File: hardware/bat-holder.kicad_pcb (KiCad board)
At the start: 2 copper layers, 85 x 56 mm, 30 parts, among them J101 BAT_1049P, K101 BAT, K102 NTC, P101 C, Q101 NPN, Q102 NPN, Q103 DMP2035UVTQ, Q104 DMP2035UVTQ, U101 AP9211

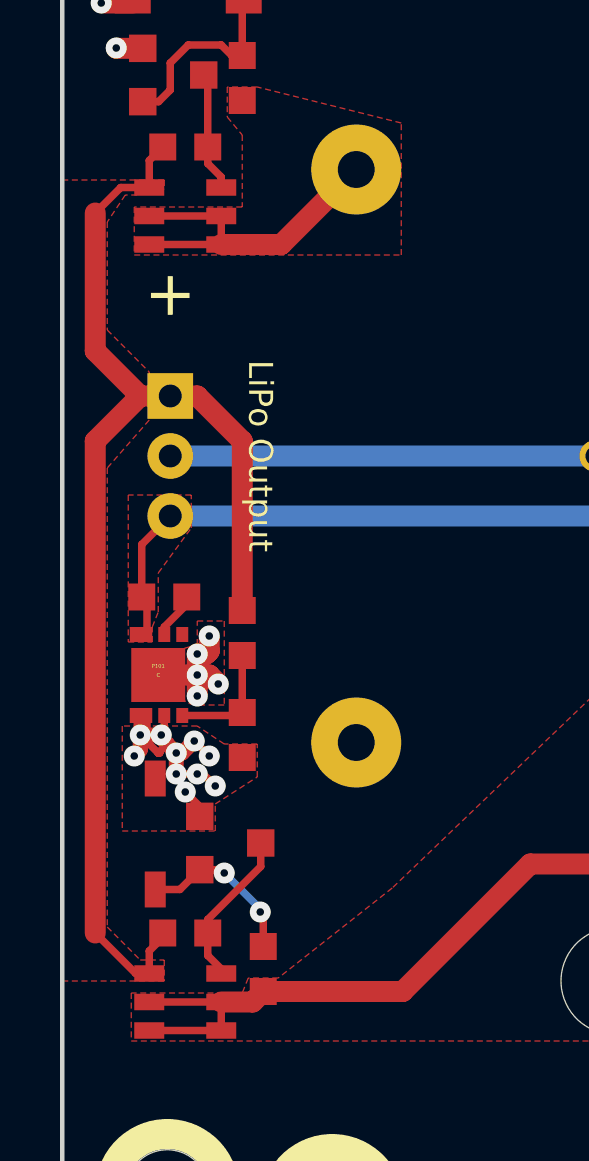
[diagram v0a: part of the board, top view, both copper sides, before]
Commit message: add debugging resistors
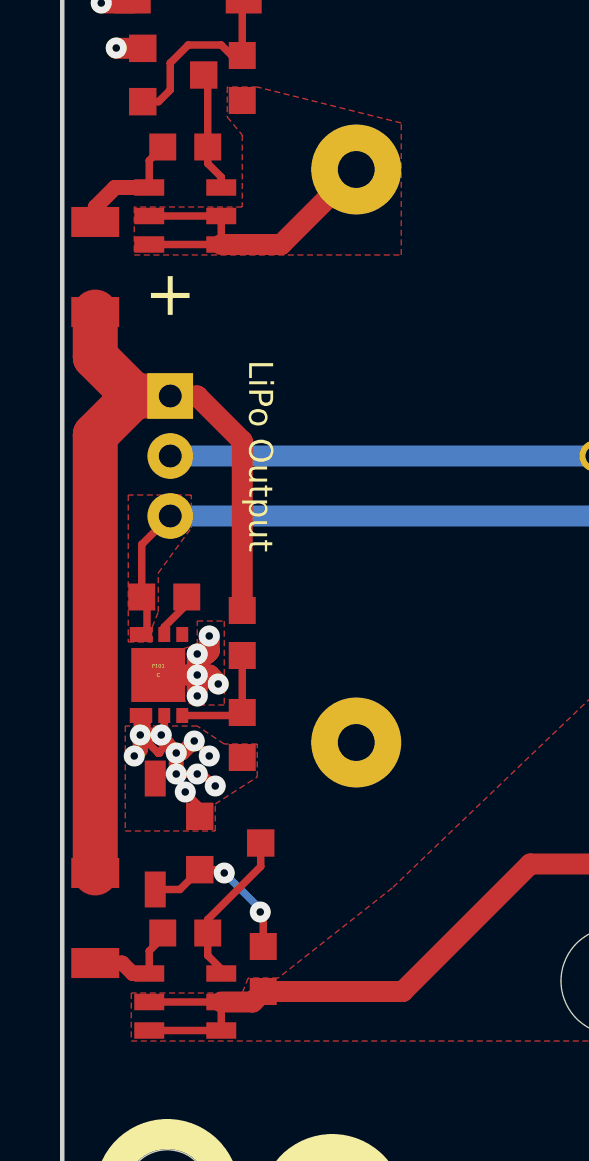
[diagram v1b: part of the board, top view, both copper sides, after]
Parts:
- added R107: 0, R1206, F.Cu at (74.1, 97.7)
- added R108: 0, R1206, F.Cu at (74.1, 119.4)
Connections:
- Q103 pad S: OUT -> OUT1
- Q104 pad S: OUT -> OUT2
- R103 pad 2: OUT -> OUT1
- R104 pad 2: OUT -> OUT2
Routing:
- net OUT: track 42.5 -> 50.5 mm
- net OUT1: track 0.00 -> 6.26 mm
- net OUT2: track 0.00 -> 3.48 mm
- removed copper zone on F.Cu, net OUT
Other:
- rule pad_to_mask_clearance: 0.051 -> 0
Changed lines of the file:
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@@
     (thickness 1.6)
     (drawings 23)
-    (tracks 127)
+    (tracks 137)
     (zones 0)
-    (modules 30)
-    (nets 14)
+    (modules 32)
+    (nets 16)
   )
   (page A4)
@@
   )
   (setup
-    (last_trace_width 0.7)
+    (last_trace_width 0.15)
     (user_trace_width 0.2)
     (user_trace_width 0.25)
@@
     (pad_size 0.1 0.1)
     (pad_drill 0)
-    (pad_to_mask_clearance 0.051)
-    (solder_mask_min_width 0.25)
+    (pad_to_mask_clearance 0)
     (aux_axis_origin 73 76)
     (grid_origin 73 76)
@@
   (net 12 VBAT2)
   (net 13 VBAT1)
+  (net 14 OUT1)
+  (net 15 OUT2)
   (net_class Default "This is the default net class."
     (clearance 0.15)
@@
     (add_net "Net-(R106-Pad2)")
     (add_net OUT)
+    (add_net OUT1)
+    (add_net OUT2)
     (add_net VBAT1)
     (add_net VBAT2)
@@
       (net 13 VBAT1))
     (pad S smd rect (at 0.95 -1.2 90) (size 0.55 1) (layers F.Cu F.Paste F.Mask)
-      (net 6 OUT))
+      (net 14 OUT1))
     (pad G smd rect (at 0.95 1.2 90) (size 0.55 1) (layers F.Cu F.Paste F.Mask)
       (net 8 "Net-(Q101-PadC)"))
@@
       (net 9 "Net-(Q102-PadC)"))
     (pad S smd rect (at 0.95 -1.2 90) (size 0.55 1) (layers F.Cu F.Paste F.Mask)
-      (net 6 OUT))
+      (net 15 OUT2))
     (pad D smd rect (at 0 -1.2 90) (size 0.55 1) (layers F.Cu F.Paste F.Mask)
       (net 12 VBAT2))
@@
       (net 8 "Net-(Q101-PadC)"))
     (pad 2 smd rect (at 0.75 0 180) (size 0.9 0.9) (layers F.Cu F.Paste F.Mask)
-      (net 6 OUT))
+      (net 14 OUT1))
     (model Resistors_SMD/R_0603.wrl
       (at (xyz 0 0 0))
@@
       (net 9 "Net-(Q102-PadC)"))
     (pad 2 smd rect (at 0.75 0 180) (size 0.9 0.9) (layers F.Cu F.Paste F.Mask)
-      (net 6 OUT))
+      (net 15 OUT2))
     (model Resistors_SMD/R_0603.wrl
       (at (xyz 0 0 0))
@@
     )
   )
+  (module R1206 (layer F.Cu)
+    (at 74.1 97.7 270)
+    (attr smd)
+    (fp_text reference R107 (at 0 0.5375 270) (layer F.Fab)
+      (effects (font (size 0.3 0.3) (thickness 0.075)))
+    )
+    (fp_text value 0 (at 0 -0.65 270) (layer F.Fab)
+      (effects (font (size 0.3 0.3) (thickness 0.075)))
+    )
+    (fp_line (start 2.25044 -1.09982) (end -2.25044 -1.09982) (layer F.Fab) (width 0.001))
+    (fp_line (start 2.25044 1.09982) (end 2.25044 -1.09982) (layer F.Fab) (width 0.001))
+    (fp_line (start -2.25044 1.09982) (end 2.25044 1.09982) (layer F.Fab) (width 0.001))
+    (fp_line (start -2.25044 -1.09982) (end -2.25044 1.09982) (layer F.Fab) (width 0.001))
+    (pad 2 smd rect (at 1.50114 0 270) (size 1.00076 1.6002) (layers F.Cu F.Paste F.Mask)
+      (net 6 OUT))
+    (pad 1 smd rect (at -1.50114 0 270) (size 1.00076 1.6002) (layers F.Cu F.Paste F.Mask)
+      (net 14 OUT1))
+    (model Resistors_SMD/R_1206.wrl
+      (at (xyz 0 0 0))
+      (scale (xyz 1 1 1))
+      (rotate (xyz 0 0 0))
+    )
+  )
+  (module R1206 (layer F.Cu)
+    (at 74.1 119.4 90)
+    (attr smd)
+    (fp_text reference R108 (at 0 0.5375 90) (layer F.Fab)
+      (effects (font (size 0.3 0.3) (thickness 0.075)))
+    )
+    (fp_text value 0 (at 0 -0.65 90) (layer F.Fab)
+      (effects (font (size 0.3 0.3) (thickness 0.075)))
+    )
+    (fp_line (start -2.25044 -1.09982) (end -2.25044 1.09982) (layer F.Fab) (width 0.001))
+    (fp_line (start -2.25044 1.09982) (end 2.25044 1.09982) (layer F.Fab) (width 0.001))
+    (fp_line (start 2.25044 1.09982) (end 2.25044 -1.09982) (layer F.Fab) (width 0.001))
+    (fp_line (start 2.25044 -1.09982) (end -2.25044 -1.09982) (layer F.Fab) (width 0.001))
+    (pad 1 smd rect (at -1.50114 0 90) (size 1.00076 1.6002) (layers F.Cu F.Paste F.Mask)
+      (net 15 OUT2))
+    (pad 2 smd rect (at 1.50114 0 90) (size 1.00076 1.6002) (layers F.Cu F.Paste F.Mask)
+      (net 6 OUT))
+    (model Resistors_SMD/R_1206.wrl
+      (at (xyz 0 0 0))
+      (scale (xyz 1 1 1))
+      (rotate (xyz 0 0 0))
+    )
+  )
   (gr_text + (at 146 128) (layer F.SilkS)
     (effects (font (size 3 3) (thickness 0.3)))
@@
   (segment (start 75.35088 88.9) (end 74.3 88.9) (width 0.7) (layer F.Cu) (net 5) (status 400000))
   (via (at 74.3 88.9) (size 0.7) (drill 0.25) (layers F.Cu B.Cu) (net 5))
-  (segment (start 75.9 121.25) (end 75.45 121.25) (width 0.25) (layer F.Cu) (net 6) (status C00000))
-  (segment (start 74.1 103.5) (end 75.6 102) (width 0.7) (layer F.Cu) (net 6))
-  (segment (start 74.1 119.9) (end 74.1 103.5) (width 0.7) (layer F.Cu) (net 6))
-  (segment (start 75.45 121.25) (end 74.1 119.9) (width 0.25) (layer F.Cu) (net 6) (status 400000))
-  (segment (start 76.35 119.9) (end 76.35 120.05) (width 0.25) (layer F.Cu) (net 6) (status C00000))
-  (segment (start 75.9 120.5) (end 75.9 121.25) (width 0.25) (layer F.Cu) (net 6) (status 800000))
-  (segment (start 76.35 120.05) (end 75.9 120.5) (width 0.25) (layer F.Cu) (net 6) (status 400000))
   (segment (start 79 109.15) (end 79 103.5) (width 0.7) (layer F.Cu) (net 6) (status 400000))
   (segment (start 77.5 102) (end 76.6 102) (width 0.7) (layer F.Cu) (net 6) (status 800000))
   (segment (start 79 103.5) (end 77.5 102) (width 0.7) (layer F.Cu) (net 6))
-  (segment (start 76.6 102) (end 75.6 102) (width 0.7) (layer F.Cu) (net 6) (status 400000))
-  (segment (start 75.6 102) (end 74.1 100.5) (width 0.7) (layer F.Cu) (net 6))
-  (segment (start 74.1 100.5) (end 74.1 95.9) (width 0.7) (layer F.Cu) (net 6))
-  (segment (start 74.1 95.9) (end 74.95 95.05) (width 0.25) (layer F.Cu) (net 6))
-  (segment (start 74.95 95.05) (end 75.9 95.05) (width 0.25) (layer F.Cu) (net 6) (status 800000))
-  (segment (start 75.9 95.05) (end 75.9 94.15) (width 0.25) (layer F.Cu) (net 6) (status C00000))
-  (segment (start 75.9 94.15) (end 76.35 93.7) (width 0.25) (layer F.Cu) (net 6) (status C00000))
+  (segment (start 74.1 117.89886) (end 74.1 103.5) (width 0.5) (layer F.Cu) (net 6) (status 400000))
+  (segment (start 76.2 101.6) (end 76.6 102) (width 0.5) (layer F.Cu) (net 6) (status C00000))
+  (segment (start 76 101.6) (end 76.2 101.6) (width 0.5) (layer F.Cu) (net 6) (status C00000))
+  (segment (start 74.1 103.5) (end 76 101.6) (width 0.5) (layer F.Cu) (net 6) (status 800000))
+  (segment (start 76.6 102) (end 75.4 102) (width 0.5) (layer F.Cu) (net 6) (status 400000))
+  (segment (start 75.4 102) (end 74.1 100.7) (width 0.5) (layer F.Cu) (net 6))
+  (segment (start 74.1 99.20114) (end 74.1 100.7) (width 1.5) (layer F.Cu) (net 6) (status 400000))
+  (segment (start 74.1 100.7) (end 75.4 102) (width 1.5) (layer F.Cu) (net 6))
+  (segment (start 75.4 102) (end 76.6 102) (width 1.5) (layer F.Cu) (net 6) (status 800000))
+  (segment (start 74.1 117.89886) (end 74.1 103.3) (width 1.5) (layer F.Cu) (net 6) (status 400000))
+  (segment (start 74.1 103.3) (end 75.4 102) (width 1.5) (layer F.Cu) (net 6))
   (segment (start 79 90.65) (end 78.65 90.65) (width 0.25) (layer F.Cu) (net 7) (status C00000))
   (segment (start 76.211 92.189) (end 75.684 92.189) (width 0.25) (layer F.Cu) (net 7) (status 800000))
@@
   (segment (start 78.3 96) (end 78.3 96.95) (width 0.25) (layer F.Cu) (net 13) (status C00000))
   (segment (start 75.9 96.95) (end 78.3 96.95) (width 0.25) (layer F.Cu) (net 13) (status C00000))
+  (segment (start 74.1 95.9) (end 74.95 95.05) (width 0.25) (layer F.Cu) (net 14))
+  (segment (start 74.95 95.05) (end 75.9 95.05) (width 0.25) (layer F.Cu) (net 14) (status 800000))
+  (segment (start 75.9 95.05) (end 75.9 94.15) (width 0.25) (layer F.Cu) (net 14) (status C00000))
+  (segment (start 75.9 94.15) (end 76.35 93.7) (width 0.25) (layer F.Cu) (net 14) (status C00000))
+  (segment (start 75.9 95.05) (end 74.75 95.05) (width 0.5) (layer F.Cu) (net 14) (status 400000))
+  (segment (start 74.1 95.7) (end 74.1 96.19886) (width 0.5) (layer F.Cu) (net 14) (status C00000))
+  (segment (start 74.75 95.05) (end 74.1 95.7) (width 0.5) (layer F.Cu) (net 14) (status 800000))
+  (segment (start 76.35 119.9) (end 76.35 120.05) (width 0.25) (layer F.Cu) (net 15) (status C00000))
+  (segment (start 75.9 120.5) (end 75.9 121.25) (width 0.25) (layer F.Cu) (net 15) (status 800000))
+  (segment (start 76.35 120.05) (end 75.9 120.5) (width 0.25) (layer F.Cu) (net 15) (status 400000))
+  (segment (start 75.9 121.25) (end 75.35 121.25) (width 0.5) (layer F.Cu) (net 15) (status 400000))
+  (segment (start 75.00114 120.90114) (end 74.1 120.90114) (width 0.5) (layer F.Cu) (net 15) (status 800000))
+  (segment (start 75.35 121.25) (end 75.00114 120.90114) (width 0.5) (layer F.Cu) (net 15))
   (zone (net 5) (net_name GBAT) (layer B.Cu) (hatch edge 0.508)
     (connect_pads yes (clearance 0.4))
@@
       (pts
         (xy 78.1 116.5) (xy 78.1 115.6) (xy 79.5 114.7) (xy 79.5 113.6) (xy 78.4 113.6)
-        (xy 77.5 113) (xy 75 113) (xy 75 116.5)
+        (xy 77.5 113) (xy 75.1 113) (xy 75.1 116.5)
       )
     )
@@
       )
     )
-  )
-  (zone (net 6) (net_name OUT) (layer F.Cu) (hatch edge 0.508)
-    (connect_pads yes (clearance 0.4))
-    (min_thickness 0.15)
-    (fill yes (arc_segments 16) (thermal_gap 0.15) (thermal_bridge_width 0.7))
-    (polygon
-      (pts
-        (xy 76.4 121.5) (xy 73 121.5) (xy 73 94.8) (xy 76.4 94.8) (xy 76.4 95.1)
-        (xy 75.5 95.3) (xy 75.1 95.3) (xy 74.5 96.2) (xy 74.5 99.8) (xy 75.9 101.2)
-        (xy 75.9 102.8) (xy 74.5 104.4) (xy 74.5 119.7) (xy 75.6 120.8) (xy 76.4 120.8)
-      )
-    )

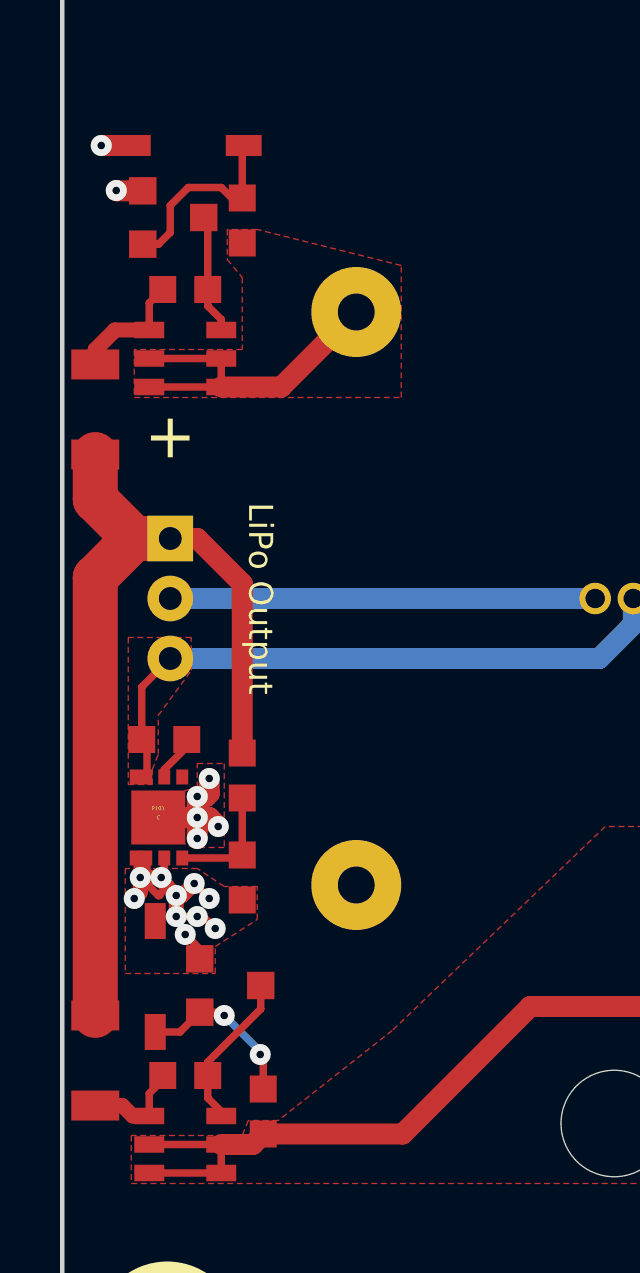
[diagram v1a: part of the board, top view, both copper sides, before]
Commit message: fix bc846 footprints, fix connector orientation
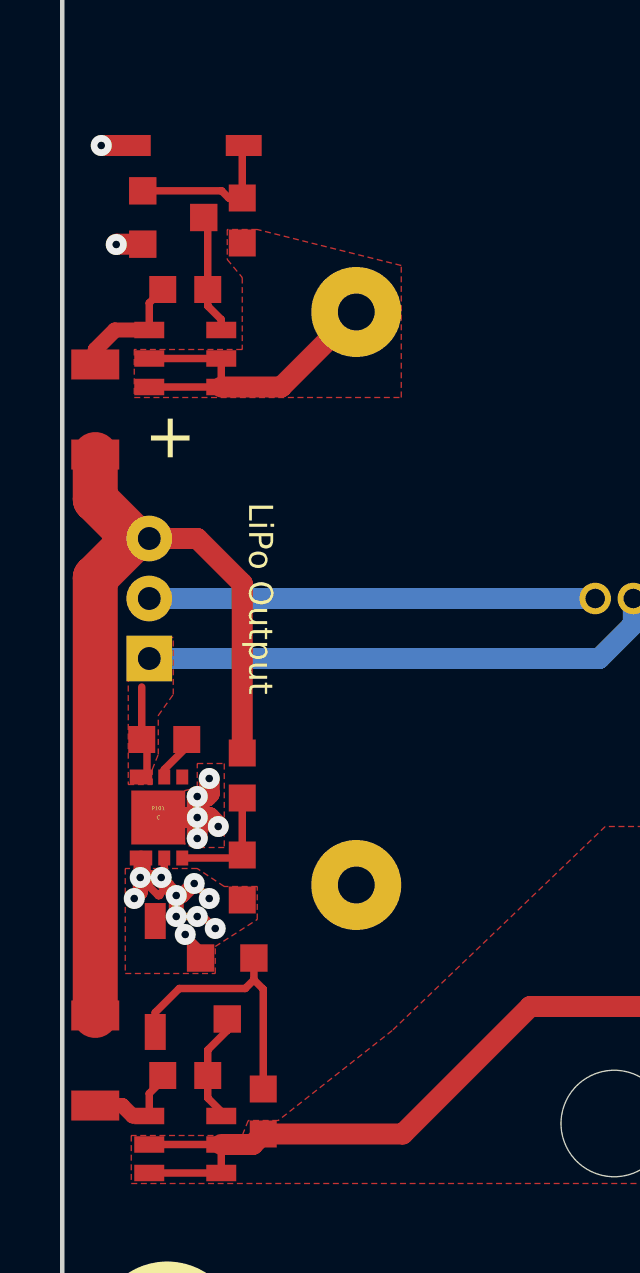
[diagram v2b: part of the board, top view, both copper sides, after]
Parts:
- Q101, Q102: value NPN -> BC846; footprint SOT23EBC -> kicad-libraries:SOT23EBC
- moved K101 0.70 mm to (75.9, 104.0), turned to 270 degrees
- moved Q102 0.14 mm to (78.5, 117.0), turned to 0 degrees
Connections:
- K101 pad 1: OUT -> GND
- K101 pad 3: GND -> OUT
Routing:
- net Net-(D102-Pad2): track 5.61 -> 8.88 mm, vias 2 -> 0
- net Net-(Q102-PadC): track 5.27 -> 3.69 mm
- net Net-(D101-Pad2): track 6.54 -> 5.19 mm
- net GND: track 21.3 -> 19.9 mm

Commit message: routing nearly completed
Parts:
- removed G***: LOGO, kicad-libraries:TF_LOGO_70MM
- removed G***: Logo_31x31, kicad-libraries:Logo_31x31
- removed K102: NTC, kicad-libraries:Pin_Header_Straight_1x02_127
- removed R105: 330, R0603F
- removed R106: 2.7k, R0603F
- removed REF** (x4): DRILL_26, kicad-libraries:DRILL_26
- removed VAL: CE_5mm, kicad-libraries:CE_5mm
- removed VAL: WEEE_7mm, kicad-libraries:WEEE_7mm
- removed ~4 (x4): DRILL, kicad-libraries:DRILL_NP
- added C102: 100nF, C0603F, F.Cu at (83.7, 95.4)
- added C103: 220pF, C0402F, F.Cu at (81.9, 102.0)
- added C104: 100nF/16V, kicad-libraries:C0603F, F.Cu at (87.6, 95.4)
- added C105: 470nF, kicad-libraries:C0603F, F.Cu at (87.6, 96.7)
- added C106: 470µF/16V, kicad-libraries:ELKO_83, F.Cu at (112.0, 118.1)
- added C107: 1uF, kicad-libraries:C0603F, F.Cu at (91.8, 89.1)
- added C108: 1uF, kicad-libraries:C0603F, F.Cu at (87.2, 89.1)
- added C201: 10uF, kicad-libraries:C1206, F.Cu at (131.8, 84.7)
- added C202: 10uF, kicad-libraries:C1206, F.Cu at (129.6, 84.7)
- added C203: 10uF, kicad-libraries:C1206, F.Cu at (134.0, 84.7)
- added C204: 100nF/16V, kicad-libraries:C0603F, F.Cu at (136.4, 96.7)
- added C205: 2.2uF, kicad-libraries:C0603F, F.Cu at (144.9, 97.9)
- added C206: UWT1H221MNL1GS, kicad-libraries:ELKO_103, F.Cu at (98.4, 110.6)
- added C207: 100nF/16V, kicad-libraries:C0603F, F.Cu at (139.5, 95.6)
- added C208: 10uF, C1206, F.Cu at (104.9, 109.2)
- added C209: 100nF, C0603F, F.Cu at (106.7, 108.5)
- added C210: 8.2nF, kicad-libraries:C0603F, F.Cu at (136.4, 98.1)
- added C211: 100pF, C0603F, F.Cu at (109.8, 108.5)
- added C212: 36pF, kicad-libraries:C0603F, F.Cu at (144.5, 101.7)
- added C213: 680pF, kicad-libraries:C0603F, F.Cu at (144.5, 103.3)
- added C214: 10uF, kicad-libraries:C1206, F.Cu at (137.6, 105.1)
- added C215: 10uF, kicad-libraries:C1206, F.Cu at (142.1, 105.1)
- added C216: 10uF, kicad-libraries:C1206, F.Cu at (137.6, 107.3)
- added C217: 10uF, kicad-libraries:C1206, F.Cu at (142.1, 107.3)
- added C218: 10uF, kicad-libraries:C1206, F.Cu at (137.6, 109.5)
- added C219: 4.7nF, C0603F, F.Cu at (102.8, 98.0)
- added C220: 100nF, C0603F, F.Cu at (129.2, 110.6)
- added C221: 10uF, kicad-libraries:C1206, F.Cu at (111.1, 82.5)
- added C222: 100nF/16V, kicad-libraries:C0603F, F.Cu at (112.9, 83.3)
- added C223: 10uF, C1206, F.Cu at (129.9, 112.4)
- added C224: 100nF/16V, kicad-libraries:C0603F, F.Cu at (112.1, 89.8)
- added C225: 470µF/16V, kicad-libraries:ELKO_83, F.Cu at (125.5, 118.1)
- added C226: 1uF, kicad-libraries:C0603F, F.Cu at (111.8, 86.3)
- added C227: DNP, C0603F, F.Cu at (128.2, 124.5)
- added C228: 100nF, kicad-libraries:C0603F, F.Cu at (120.6, 85.6)
- added C229: 470µF/16V, kicad-libraries:ELKO_83, F.Cu at (105.4, 87.5)
- added C230: 100nF, kicad-libraries:C0603F, F.Cu at (120.5, 88.0)
- added C231: 10uF, C1206, F.Cu at (124.4, 88.8)
- added C232: 10uF, C1206, F.Cu at (122.2, 88.8)
- added C233: 470µF/16V, kicad-libraries:ELKO_83, F.Cu at (139.0, 118.1)
- added D103: blue, D0603F, F.Cu at (87.6, 77.5)
- added D104: green, D0603F, F.Cu at (93.7, 77.5)
- added D105: green, D0603F, F.Cu at (96.7, 77.5)
- added D106: green, D0603F, F.Cu at (99.7, 77.5)
- added D107: B0520LW-7, SOD-123, F.Cu at (76.7, 95.1)
- added D201: Z12V, SOD-123, F.Cu at (86.6, 113.4)
- added D202: PMEG6045, SOD-128, F.Cu at (137.1, 112.0)
- added D203: PMEG6045, SOD-128, F.Cu at (110.4, 111.6)
- added D204: PMEG6045, SOD-128, F.Cu at (132.3, 124.0)
- added J102: USB-A, kicad-libraries:USB-A-SMT-8231, F.Cu at (98.0, 124.5)
- added L201: 1uH 74437368010, WE-LHMI, F.Cu at (140.8, 87.9)
- added L202: 22uH 74437368220, WE-LHMI, F.Cu at (122.1, 108.1)
- added L203: 4.7uH 7447789004, WE-PD, F.Cu at (118.0, 81.1)
- added P102: DEBUG, kicad-libraries:DEBUG_PAD, F.Cu at (78.1, 83.9)
- added P103: CON-SENSOR2, kicad-libraries:CON-SENSOR2, F.Cu at (73.0, 104.0)
- added P104: C, TSTPT, F.Cu at (86.3, 93.3)
- added P105: 5V Out, kicad-libraries:OQ_2P, F.Cu at (112.0, 124.0)
- added P201: Input, kicad-libraries:OQ_2P, F.Cu at (84.0, 124.0)
- added Q201: Si4447ADY, kicad-libraries:SOIC-8-MOSFET, F.Cu at (90.1, 114.2)
- added R109: DNP, kicad-libraries:R0603F, F.Cu at (92.4, 98.3)
- added R110: 10m, kicad-libraries:R1210, F.Cu at (91.7, 92.7)
- added R201: VC120626D580DP, R1206, F.Cu at (87.0, 120.0)
- added R202: 10k, kicad-libraries:R0603F, F.Cu at (84.4, 117.6)
- added R203: 1k, kicad-libraries:R0603F, F.Cu at (84.4, 116.3)
- added R204: 10k, kicad-libraries:R0603F, F.Cu at (85.2, 114.1)
- added R205: 332k, kicad-libraries:R0603F, F.Cu at (142.0, 95.6)
- added R206: 105k TBD, kicad-libraries:R0603F, F.Cu at (144.9, 100.3)
- added R207: 27, R0603F, F.Cu at (109.8, 107.2)
- added R208: 36.5k, kicad-libraries:R0603F, F.Cu at (142.4, 102.5)
- added R209: 309k, kicad-libraries:R0603F, F.Cu at (141.3, 109.1)
- added R210: 86.6k, kicad-libraries:R0603F, F.Cu at (144.2, 109.1)
- added R211: 20k, R0603F, F.Cu at (102.8, 103.1)
- added R212: 100, kicad-libraries:R0603F, F.Cu at (110.5, 86.3)
- added R213: 47k, R0603F, F.Cu at (126.9, 124.5)
- added R214: 8.2k, R0603F, F.Cu at (124.8, 125.3)
- added R217: 49.9k, kicad-libraries:R0603F, F.Cu at (118.3, 91.2)
- added R219: 100k, kicad-libraries:R0603F, F.Cu at (112.1, 88.5)
- added R221: 10k, kicad-libraries:R0603F, F.Cu at (119.6, 91.2)
- added RP101: 1k, kicad-libraries:4X0402, F.Cu at (87.7, 80.8)
- added RP102: 82, kicad-libraries:4X0402, F.Cu at (80.3, 102.0)
- added RP103: 10k, kicad-libraries:4X0402, F.Cu at (83.3, 78.6)
- added RP201: 1k, kicad-libraries:4X0603, F.Cu at (115.8, 91.2)
- added U102: AP9211, DFN2030-6, F.Cu at (86.3, 93.3)
- added U103: MAX17260_LS, kicad-libraries:TDFN14-3x3, F.Cu at (91.7, 95.8)
- added U104: DRILL, kicad-libraries:DRILL_NP, F.Cu at (76.5, 119.0)
- added U105: DRILL, kicad-libraries:DRILL_NP, F.Cu at (151.5, 129.0)
- added U106: DRILL, kicad-libraries:DRILL_NP, F.Cu at (76.5, 89.0)
- added U107: DRILL, kicad-libraries:DRILL_NP, F.Cu at (151.5, 79.0)
- added U108: DRILL, kicad-libraries:DRILL_26, F.Cu at (76.5, 128.5)
- added U109: DRILL, kicad-libraries:DRILL_26, F.Cu at (134.5, 79.5)
- added U110: DRILL, kicad-libraries:DRILL_26, F.Cu at (76.5, 79.5)
- added U111: DRILL, kicad-libraries:DRILL_26, F.Cu at (134.5, 128.5)
- added U112: AP7333-33SA, SOT23-3, F.Cu at (89.5, 89.0)
- added U201: TPS61088RHL, VQFN20_45x35, F.Cu at (140.8, 98.6)
- added U202: BD906XX-C-HRP7, BD906XX-C-HRP7, F.Cu at (109.3, 99.4)
- added U203: AAT3620, kicad-libraries:TDFN14-3x3, F.Cu at (116.2, 86.9)
- J101: moved to B.Cu
- K101: value BAT -> NTC; footprint kicad-libraries:JST-PH-3-THT -> kicad-libraries:Pin_Header_Straight_1x02_127; moved to B.Cu
- P101: value C -> BOOT; footprint TSTPT -> kicad-libraries:SolderJumper
- Q101, Q102: footprint kicad-libraries:SOT23EBC -> SOT23EBC
- R107: value 0 -> 330; footprint R1206 -> R0603F
- R108: value 0 -> 2.7k; footprint R1206 -> R0603F
- U101: value AP9211 -> XMC1XXX24; footprint DFN2030-6 -> kicad-libraries:QFN24-4x4mm-0.5mm
- moved R101 77.6 mm to (156.5, 88.0)
- moved Q101 77.5 mm to (153.9, 84.1)
- moved Q103 77.1 mm to (153.9, 88.7)
- moved R103 77.1 mm to (153.9, 86.4)
- moved D101 73.8 mm to (150.9, 85.1), turned to 90 degrees
- moved P101 31.4 mm to (80.6, 80.2)
- moved R108 30.4 mm to (88.8, 92.8), turned to 270 degrees
- moved C101 29.7 mm to (86.8, 84.6)
- moved U101 27.4 mm to (82.8, 84.7), turned to 90 degrees
- moved R102 18.0 mm to (89.2, 105.8)
- moved D102 17.1 mm to (86.8, 103.2), turned to 0 degrees
- moved R104 15.9 mm to (84.4, 105.8), turned to 270 degrees
- moved Q104 15.7 mm to (85.6, 109.0)
- moved K101 15.5 mm to (91.3, 102.3), turned to 90 degrees
- moved Q102 13.9 mm to (86.8, 105.8)
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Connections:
- C101 pad 1: Net-(C101-Pad1) -> 3V3
- C101 pad 2: GBAT -> GND
- K101 pad 1: GND -> Net-(K101-Pad1)
- K101 pad 2: Net-(K101-Pad2) -> AGND
- P101 pad 1: EP1 -> GND
- Q103 pad S: OUT1 -> BAT_OUT
- Q104 pad S: OUT2 -> BAT_OUT
- R103 pad 2: OUT1 -> BAT_OUT
- R104 pad 2: OUT2 -> BAT_OUT
- R107 pad 1: OUT1 -> Net-(C102-Pad1)
- R107 pad 2: OUT -> BAT_OUT
- R108 pad 1: OUT2 -> AGND
- R108 pad 2: OUT -> Net-(R108-Pad2)
- U101 pad 1: GBAT -> SPI-MISO
- U101 pad 2: GBAT -> DC-IN-VOLTAGE
- U101 pad 3: Net-(C101-Pad1) -> (no net)
- U101 pad 5: Net-(R106-Pad2) -> CHARGER_STAT2
- U101 pad 6: GND -> CHARGER_STAT1
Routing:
- net VBAT2: track 86.2 -> 14.8 mm
- net +5V: track 0.00 -> 64.9 mm, vias 0 -> 8
- net GND: track 19.9 -> 75.1 mm, vias 0 -> 50
- net OUT: track 50.5 -> 0.00 mm
- net BAT_OUT: track 0.00 -> 45.9 mm, vias 0 -> 23
- net CHARGER_STAT1: track 0.00 -> 40.1 mm, vias 0 -> 2
- net DC-IN-VOLTAGE: track 0.00 -> 39.6 mm, vias 0 -> 2
- net CHARGER_STAT2: track 0.00 -> 39.2 mm, vias 0 -> 2
- net VIN2: track 0.00 -> 37.3 mm, vias 0 -> 2
- net BATTERY-SCL: track 0.00 -> 36.4 mm, vias 0 -> 2
- net CHARGER_EN: track 0.00 -> 36.0 mm, vias 0 -> 2
- net Net-(C227-Pad2): track 0.00 -> 34.0 mm, vias 0 -> 2
- net BATTERY-SDA: track 0.00 -> 26.8 mm, vias 0 -> 2
- net Net-(C214-Pad1): track 0.00 -> 23.6 mm
- net Net-(C220-Pad1): track 0.00 -> 20.8 mm
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- added copper zone on F.Cu, net +5V
- added copper zone on F.Cu, net AGND
- added copper zone on F.Cu, net BAT_OUT
- added copper zone on F.Cu, net VIN
- added copper zone on F.Cu, net VIN2
- removed copper zone on F.Cu, net EP1
- removed copper zone on B.Cu, net GBAT
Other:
- board text added: "Battery Capacity"
- board text added: "High"
- board text added: "Low"
- board text added: "Mid"
- board text added: "Status"
- board text added: "Uninterruptible Power Supply 1.0"
- board text removed: "Battery Holder 1.0"
- board text removed: "LiPo Output"
